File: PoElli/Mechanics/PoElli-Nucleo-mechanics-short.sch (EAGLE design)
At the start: 30 parts, among them J1 DF12-ELLI-HEADER-TOP, J3 M022.54MM, J4 M022.54MM, T1 Coilcraft 230NL, T2 FLYBACK750311689, U1 ENC424J600, X1 M-BOLT-2, X2 M-BOLT-2, X3 M-BOLT-2, X4 M-BOLT-2

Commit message: Changes to PoElli-Nucleo-short from today's meeting
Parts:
- T2: value FLYBACK750311689 -> FLYBACKEMBEDDED; device ELL-i-Transformers:FLYBACK750311689 -> ELL-i-Transformers:FLYBACKEMBEDDED
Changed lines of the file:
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@@
 <part name="D8" library="ELL-i-DIscreteSemi" deviceset="DIODE-SCHOTTKY" device="B2100" value="B2100"/>
 <part name="D7" library="ELL-i-DIscreteSemi" deviceset="DIODE-SCHOTTKY" device="B2100" value="B2100"/>
-<part name="T2" library="ELL-i-Transformers" deviceset="FLYBACK" device="750311689" value="FLYBACK750311689"/>
+<part name="T2" library="ELL-i-Transformers" deviceset="FLYBACK" device="EMBEDDED" value="FLYBACKEMBEDDED"/>
 <part name="J4" library="SparkFun-Connectors" deviceset="M02" device="2.54MM_SCREWTERM" value="M022.54MM"/>
 <part name="TP2" library="ELL-i-Passives" deviceset="TEST_POINT" device="-5021" value=""/>

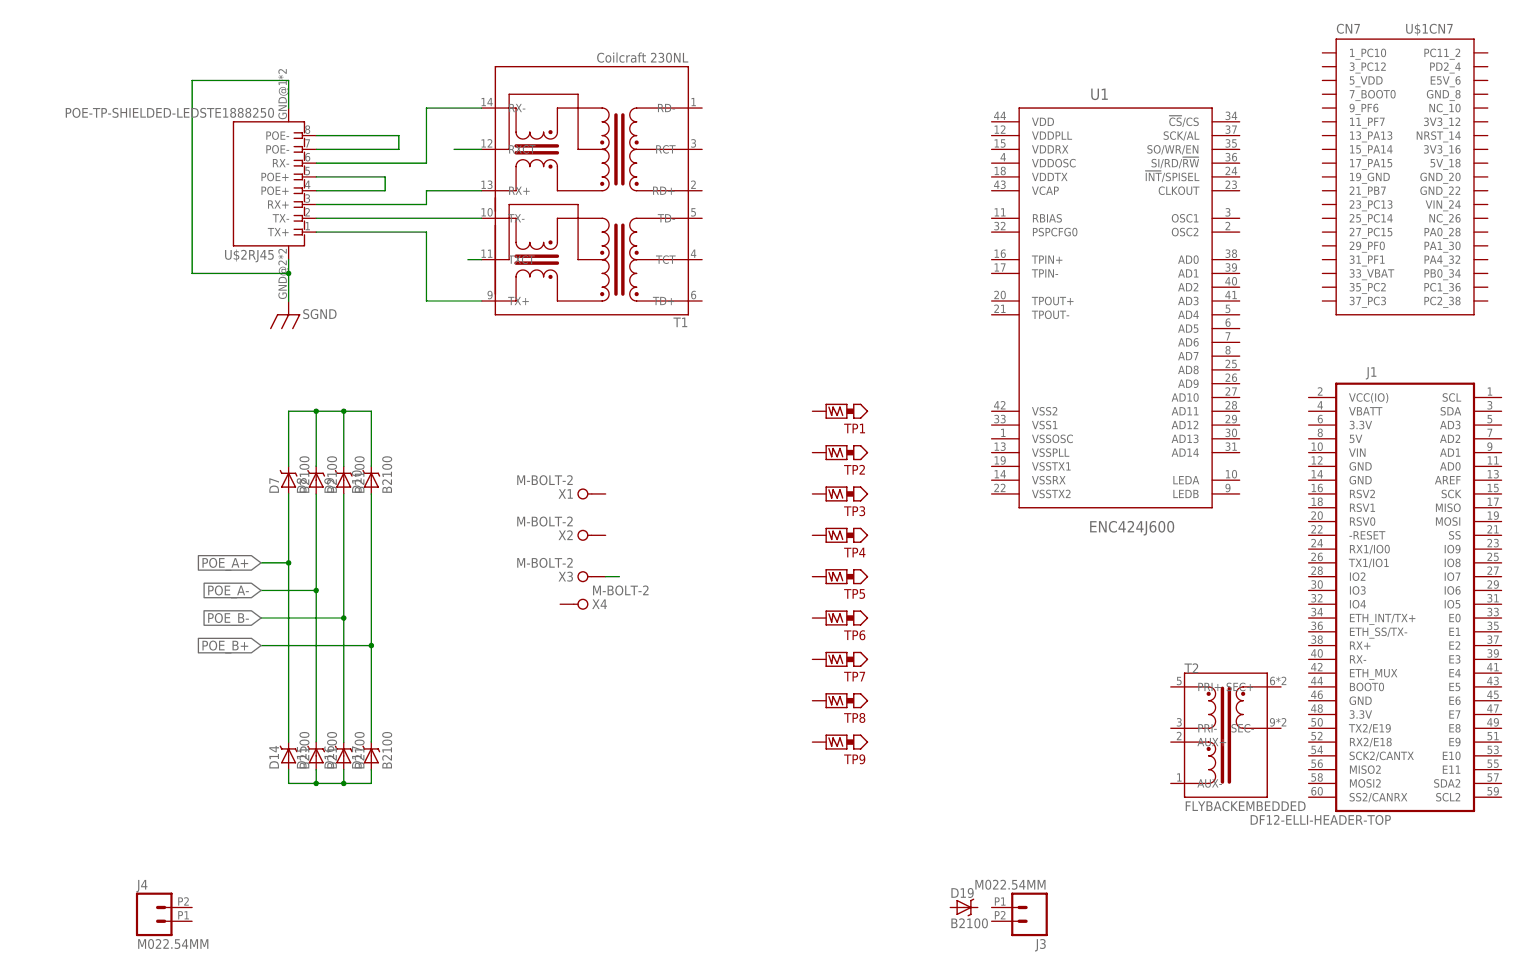
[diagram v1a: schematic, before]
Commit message: Update Nucleo shield construction for Mechanics/PoElli-Nucleo-mechanics-short.{brd,sch}
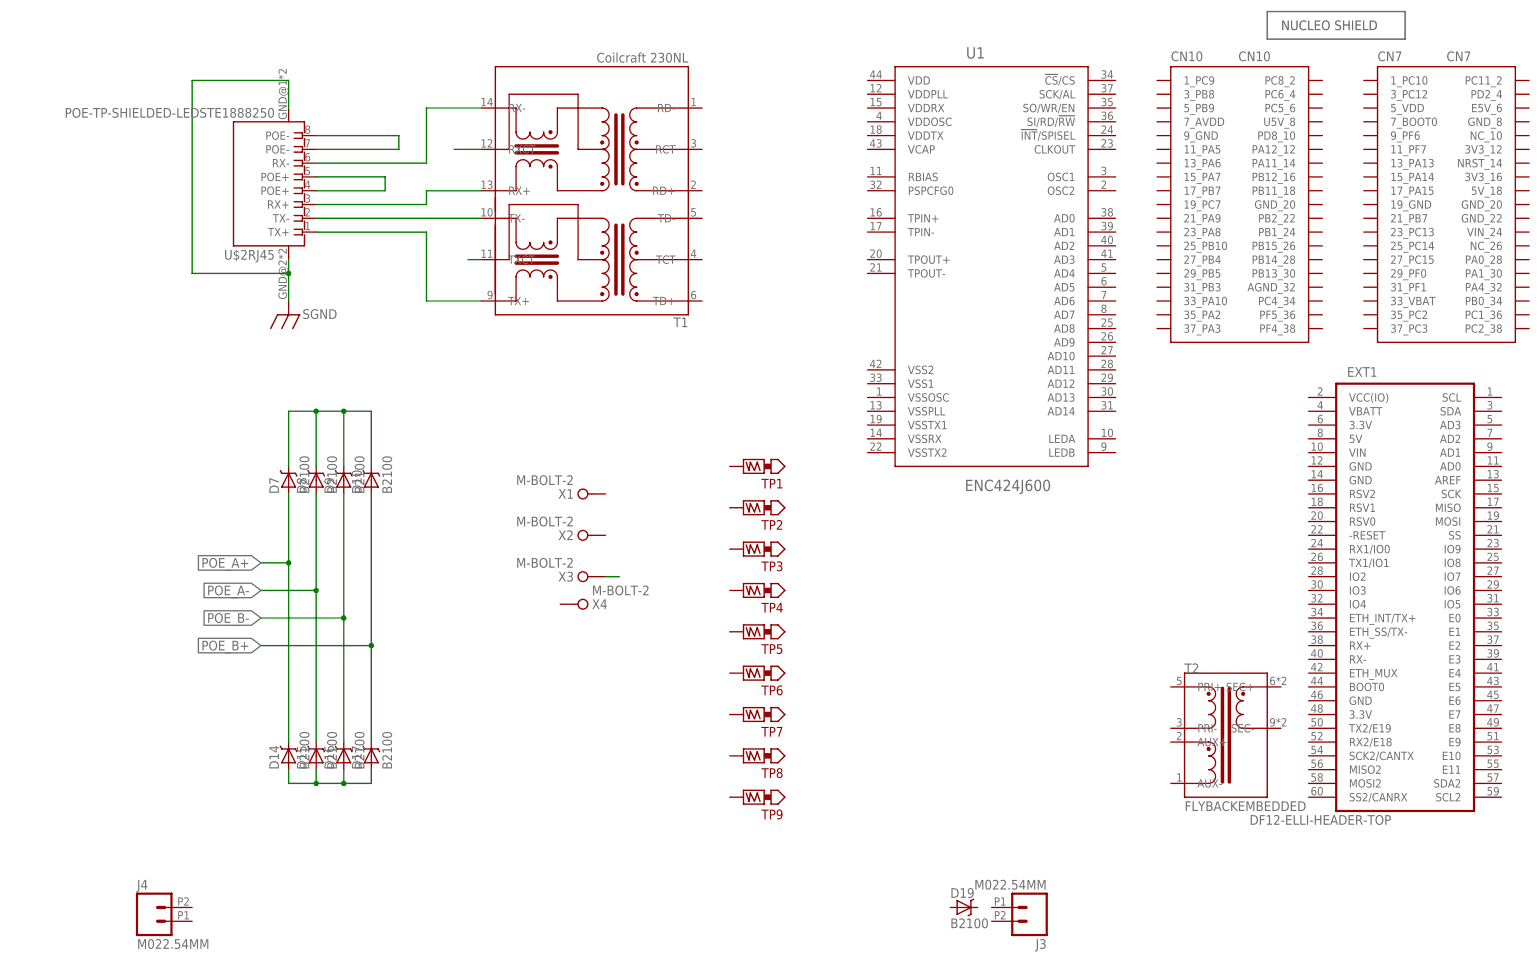
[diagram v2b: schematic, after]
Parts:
- removed U$1: NUCLEO-SHIELD, ELL-i-Boards:NUCLEO-SHIELD
- added CN10: NUCLEO-CN10, ELL-i-Boards:NUCLEO-CN10
- added CN7: NUCLEO-CN7, ELL-i-Boards:NUCLEO-CN7
- added NUCLEO: NUCLEO-OUTLINE-SHORT, ELL-i-Boards:NUCLEO-OUTLINE-SHORT
- renumbered J1 to EXT1
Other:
- moved on the sheet: TP1, TP2, TP3, TP4, TP5, TP6, TP7, TP8, TP9, U1
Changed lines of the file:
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@@
 <grid distance="0.1" unitdist="inch" unit="inch" style="lines" multiple="1" display="no" altdistance="0.01" altunitdist="inch" altunit="inch"/>
 <layers>
-<layer number="1" name="Top" color="4" fill="1" visible="yes" active="no"/>
-<layer number="16" name="Bottom" color="1" fill="1" visible="yes" active="no"/>
-<layer number="17" name="Pads" color="2" fill="1" visible="yes" active="no"/>
-<layer number="18" name="Vias" color="2" fill="1" visible="yes" active="no"/>
-<layer number="19" name="Unrouted" color="6" fill="1" visible="yes" active="no"/>
-<layer number="20" name="Dimension" color="15" fill="1" visible="yes" active="no"/>
-<layer number="21" name="tPlace" color="7" fill="1" visible="yes" active="no"/>
-<layer number="22" name="bPlace" color="7" fill="1" visible="yes" active="no"/>
-<layer number="23" name="tOrigins" color="15" fill="1" visible="yes" active="no"/>
-<layer number="24" name="bOrigins" color="15" fill="1" visible="yes" active="no"/>
-<layer number="25" name="tNames" color="7" fill="1" visible="yes" active="no"/>
-<layer number="26" name="bNames" color="7" fill="1" visible="yes" active="no"/>
-<layer number="27" name="tValues" color="7" fill="1" visible="yes" active="no"/>
-<layer number="28" name="bValues" color="7" fill="1" visible="yes" active="no"/>
+<layer number="1" name="Top" color="4" fill="1" visible="no" active="no"/>
+<layer number="16" name="Bottom" color="1" fill="1" visible="no" active="no"/>
+<layer number="17" name="Pads" color="2" fill="1" visible="no" active="no"/>
+<layer number="18" name="Vias" color="2" fill="1" visible="no" active="no"/>
+<layer number="19" name="Unrouted" color="6" fill="1" visible="no" active="no"/>
+<layer number="20" name="Dimension" color="15" fill="1" visible="no" active="no"/>
+<layer number="21" name="tPlace" color="7" fill="1" visible="no" active="no"/>
+<layer number="22" name="bPlace" color="7" fill="1" visible="no" active="no"/>
+<layer number="23" name="tOrigins" color="15" fill="1" visible="no" active="no"/>
+<layer number="24" name="bOrigins" color="15" fill="1" visible="no" active="no"/>
+<layer number="25" name="tNames" color="7" fill="1" visible="no" active="no"/>
+<layer number="26" name="bNames" color="7" fill="1" visible="no" active="no"/>
+<layer number="27" name="tValues" color="7" fill="1" visible="no" active="no"/>
+<layer number="28" name="bValues" color="7" fill="1" visible="no" active="no"/>
 <layer number="29" name="tStop" color="7" fill="3" visible="no" active="no"/>
 <layer number="30" name="bStop" color="7" fill="6" visible="no" active="no"/>
@@
 <layer number="35" name="tGlue" color="7" fill="4" visible="no" active="no"/>
 <layer number="36" name="bGlue" color="7" fill="5" visible="no" active="no"/>
-<layer number="37" name="tTest" color="7" fill="1" visible="yes" active="no"/>
-<layer number="38" name="bTest" color="7" fill="1" visible="yes" active="no"/>
+<layer number="37" name="tTest" color="7" fill="1" visible="no" active="no"/>
+<layer number="38" name="bTest" color="7" fill="1" visible="no" active="no"/>
 <layer number="39" name="tKeepout" color="4" fill="11" visible="no" active="no"/>
 <layer number="40" name="bKeepout" color="1" fill="11" visible="no" active="no"/>
@@
 <layer number="44" name="Drills" color="7" fill="1" visible="no" active="no"/>
 <layer number="45" name="Holes" color="7" fill="1" visible="no" active="no"/>
-<layer number="46" name="Milling" color="3" fill="1" visible="yes" active="no"/>
-<layer number="47" name="Measures" color="7" fill="1" visible="yes" active="no"/>
-<layer number="48" name="Document" color="7" fill="1" visible="yes" active="no"/>
-<layer number="49" name="Reference" color="7" fill="1" visible="yes" active="no"/>
-<layer number="50" name="dxf" color="7" fill="1" visible="yes" active="no"/>
-<layer number="51" name="tDocu" color="7" fill="1" visible="yes" active="no"/>
-<layer number="52" name="bDocu" color="7" fill="1" visible="yes" active="no"/>
-<layer number="53" name="tGND_GNDA" color="7" fill="9" visible="yes" active="no"/>
-<layer number="54" name="bGND_GNDA" color="1" fill="9" visible="yes" active="no"/>
-<layer number="56" name="wert" color="7" fill="1" visible="yes" active="no"/>
-<layer number="57" name="tCopper" color="7" fill="1" visible="yes" active="no"/>
-<layer number="58" name="bCopper" color="7" fill="1" visible="yes" active="no"/>
+<layer number="46" name="Milling" color="3" fill="1" visible="no" active="no"/>
+<layer number="47" name="Measures" color="7" fill="1" visible="no" active="no"/>
+<layer number="48" name="Document" color="7" fill="1" visible="no" active="no"/>
+<layer number="49" name="Reference" color="7" fill="1" visible="no" active="no"/>
+<layer number="50" name="dxf" color="7" fill="1" visible="no" active="no"/>
+<layer number="51" name="tDocu" color="7" fill="1" visible="no" active="no"/>
+<layer number="52" name="bDocu" color="7" fill="1" visible="no" active="no"/>
+<layer number="53" name="tGND_GNDA" color="7" fill="9" visible="no" active="no"/>
+<layer number="54" name="bGND_GNDA" color="1" fill="9" visible="no" active="no"/>
+<layer number="56" name="wert" color="7" fill="1" visible="no" active="no"/>
+<layer number="57" name="tCopper" color="7" fill="1" visible="no" active="no"/>
+<layer number="58" name="bCopper" color="7" fill="1" visible="no" active="no"/>
 <layer number="91" name="Nets" color="2" fill="1" visible="yes" active="yes"/>
 <layer number="92" name="Busses" color="1" fill="1" visible="yes" active="yes"/>
@@
 <parts>
 <part name="T1" library="ELL-i-Transformers" deviceset="POE-ISOLATION" device="-230NL" value="Coilcraft 230NL"/>
-<part name="J1" library="ELL-i-Connectors" deviceset="DF12-ELLI-*" device="HEADER-TOP"/>
+<part name="EXT1" library="ELL-i-Connectors" deviceset="DF12-ELLI-*" device="HEADER-TOP"/>
 <part name="D17" library="ELL-i-DIscreteSemi" deviceset="DIODE-SCHOTTKY" device="B2100" value="B2100"/>
 <part name="D16" library="ELL-i-DIscreteSemi" deviceset="DIODE-SCHOTTKY" device="B2100" value="B2100"/>
@@
 <part name="X3" library="ELL-i-Connectors" deviceset="M-BOLT" device="-2"/>
 <part name="X4" library="ELL-i-Connectors" deviceset="M-BOLT" device="-2"/>
-<part name="U$1" library="ELL-i-Boards" deviceset="NUCLEO-SHIELD" device="" value="NUCLEO-SHIELD"/>
 <part name="U1" library="ELL-i-DigitalIC" deviceset="ENC424J600" device=""/>
 <part name="U$2" library="ELL-i-Connectors" deviceset="POE-TP-SHIELDED-LEDS" device="TE1888250"/>
+<part name="CN7" library="ELL-i-Boards" deviceset="NUCLEO-CN7" device=""/>
+<part name="CN10" library="ELL-i-Boards" deviceset="NUCLEO-CN10" device=""/>
+<part name="NUCLEO" library="ELL-i-Boards" deviceset="NUCLEO-OUTLINE" device="-SHORT"/>
 </parts>
 <sheets>
@@
 <instances>
 <instance part="T1" gate="G$1" x="88.9" y="139.7" rot="R180"/>
-<instance part="J1" gate="E" x="238.76" y="68.58" rot="MR0"/>
+<instance part="EXT1" gate="E" x="238.76" y="68.58" rot="MR0"/>
 <instance part="D17" gate="G$1" x="48.26" y="38.1" rot="R90"/>
 <instance part="D16" gate="G$1" x="43.18" y="38.1" rot="R90"/>
@@
 <instance part="T2" gate="G$1" x="205.74" y="43.18"/>
 <instance part="J4" gate="G$1" x="7.62" y="7.62"/>
-<instance part="TP2" gate="TP$1" x="132.08" y="93.98" rot="R90"/>
-<instance part="TP3" gate="TP$1" x="132.08" y="86.36" rot="R90"/>
-<instance part="TP4" gate="TP$1" x="132.08" y="78.74" rot="R90"/>
-<instance part="TP5" gate="TP$1" x="132.08" y="71.12" rot="R90"/>
-<instance part="TP6" gate="TP$1" x="132.08" y="63.5" rot="R90"/>
-<instance part="TP7" gate="TP$1" x="132.08" y="55.88" rot="R90"/>
-<instance part="TP8" gate="TP$1" x="132.08" y="48.26" rot="R90"/>
-<instance part="TP9" gate="TP$1" x="132.08" y="40.64" rot="R90"/>
-<instance part="TP1" gate="TP$1" x="132.08" y="101.6" rot="R90"/>
+<instance part="TP2" gate="TP$1" x="116.84" y="83.82" rot="R90"/>
+<instance part="TP3" gate="TP$1" x="116.84" y="76.2" rot="R90"/>
+<instance part="TP4" gate="TP$1" x="116.84" y="68.58" rot="R90"/>
+<instance part="TP5" gate="TP$1" x="116.84" y="60.96" rot="R90"/>
+<instance part="TP6" gate="TP$1" x="116.84" y="53.34" rot="R90"/>
+<instance part="TP7" gate="TP$1" x="116.84" y="45.72" rot="R90"/>
+<instance part="TP8" gate="TP$1" x="116.84" y="38.1" rot="R90"/>
+<instance part="TP9" gate="TP$1" x="116.84" y="30.48" rot="R90"/>
+<instance part="TP1" gate="TP$1" x="116.84" y="91.44" rot="R90"/>
 <instance part="U$9" gate="G$1" x="0" y="0"/>
 <instance part="J3" gate="G$1" x="170.18" y="10.16" rot="R180"/>
@@
 <instance part="X3" gate="M" x="86.36" y="71.12"/>
 <instance part="X4" gate="M" x="88.138" y="66.04" rot="MR0"/>
-<instance part="U$1" gate="CN7" x="238.76" y="144.78"/>
-<instance part="U1" gate="ENC424J600" x="185.42" y="121.92"/>
+<instance part="U1" gate="ENC424J600" x="162.56" y="129.54"/>
 <instance part="U$2" gate="RJ45" x="30.48" y="142.24" rot="R180"/>
+<instance part="CN7" gate="G$1" x="246.38" y="139.7"/>
+<instance part="CN10" gate="G$1" x="208.28" y="139.7"/>
+<instance part="NUCLEO" gate="G$1" x="226.06" y="172.72"/>
 </instances>
 <busses>
